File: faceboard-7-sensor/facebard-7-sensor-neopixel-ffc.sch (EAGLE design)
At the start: 42 parts, among them J1 1-1734592-4, J3 1-1734592-4, Q1 QRE1113, Q2 QRE1113, Q3 QRE1113, Q4 QRE1113, Q5 QRE1113, Q6 QRE1113, Q7 QRE1113, U1 CD4051BE

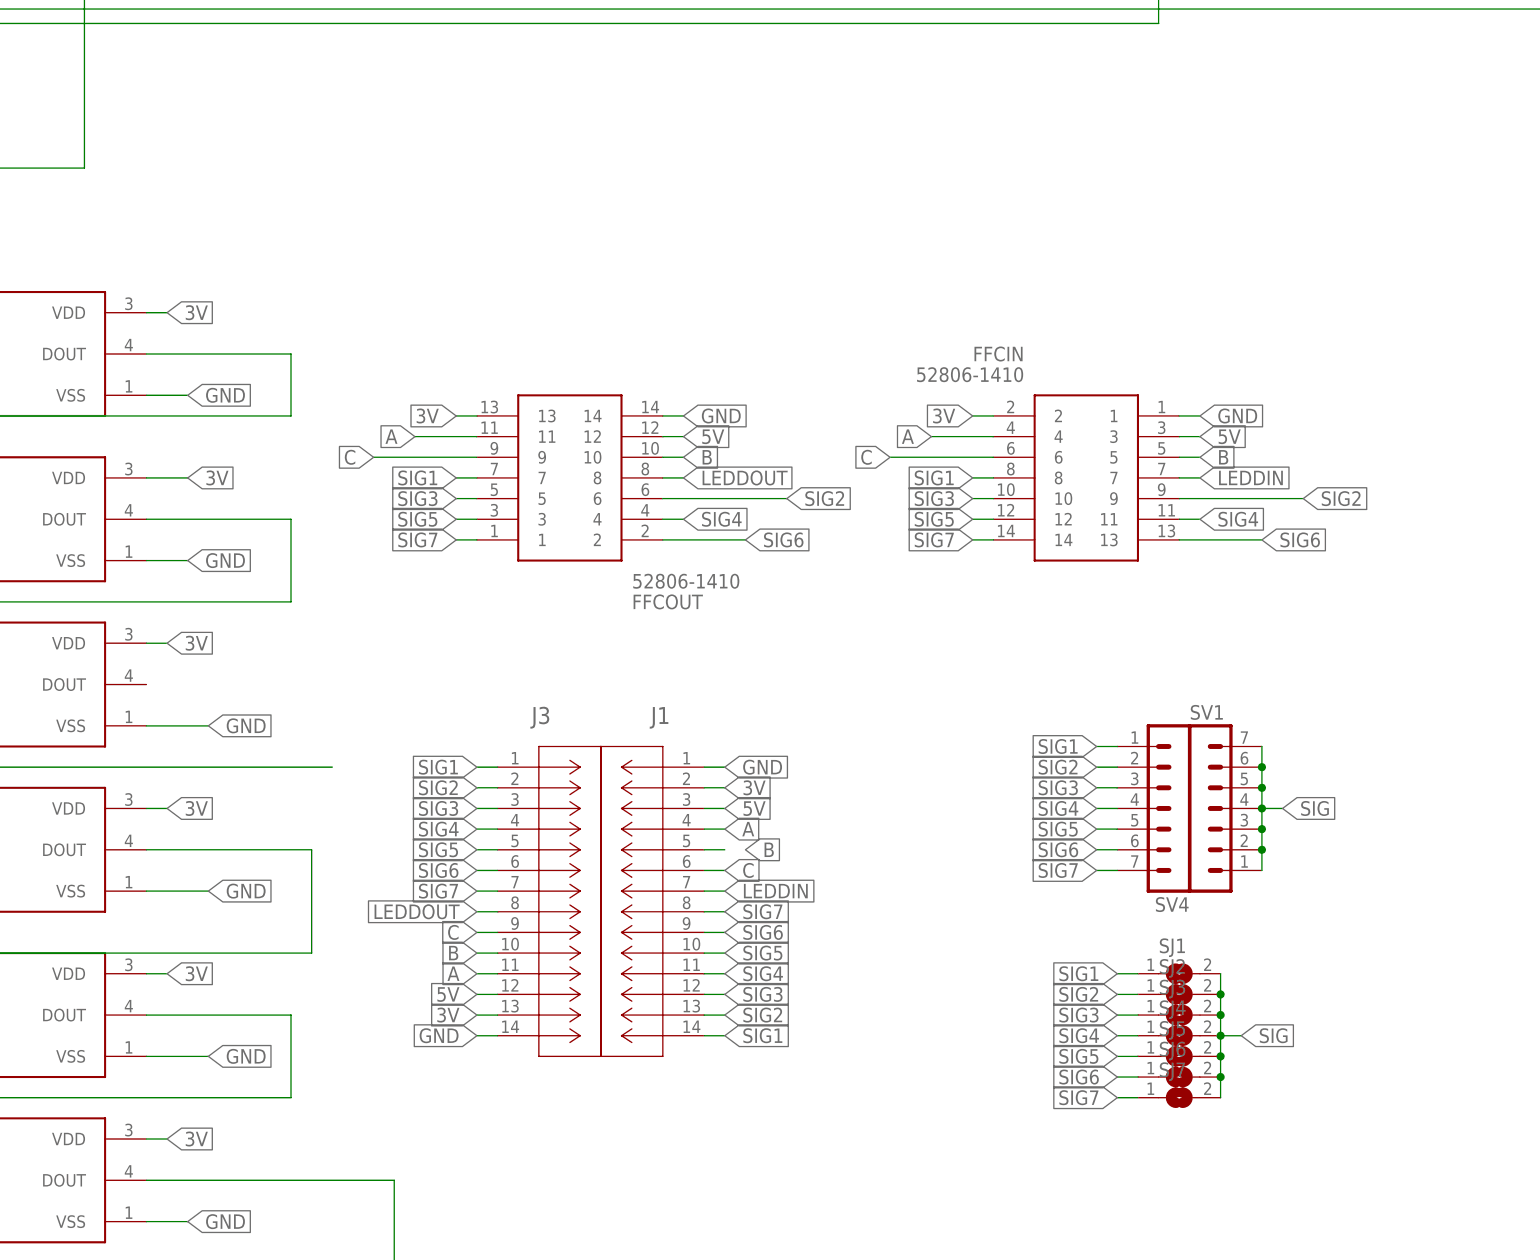
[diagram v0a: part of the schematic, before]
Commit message: remove 0.5mm ffc
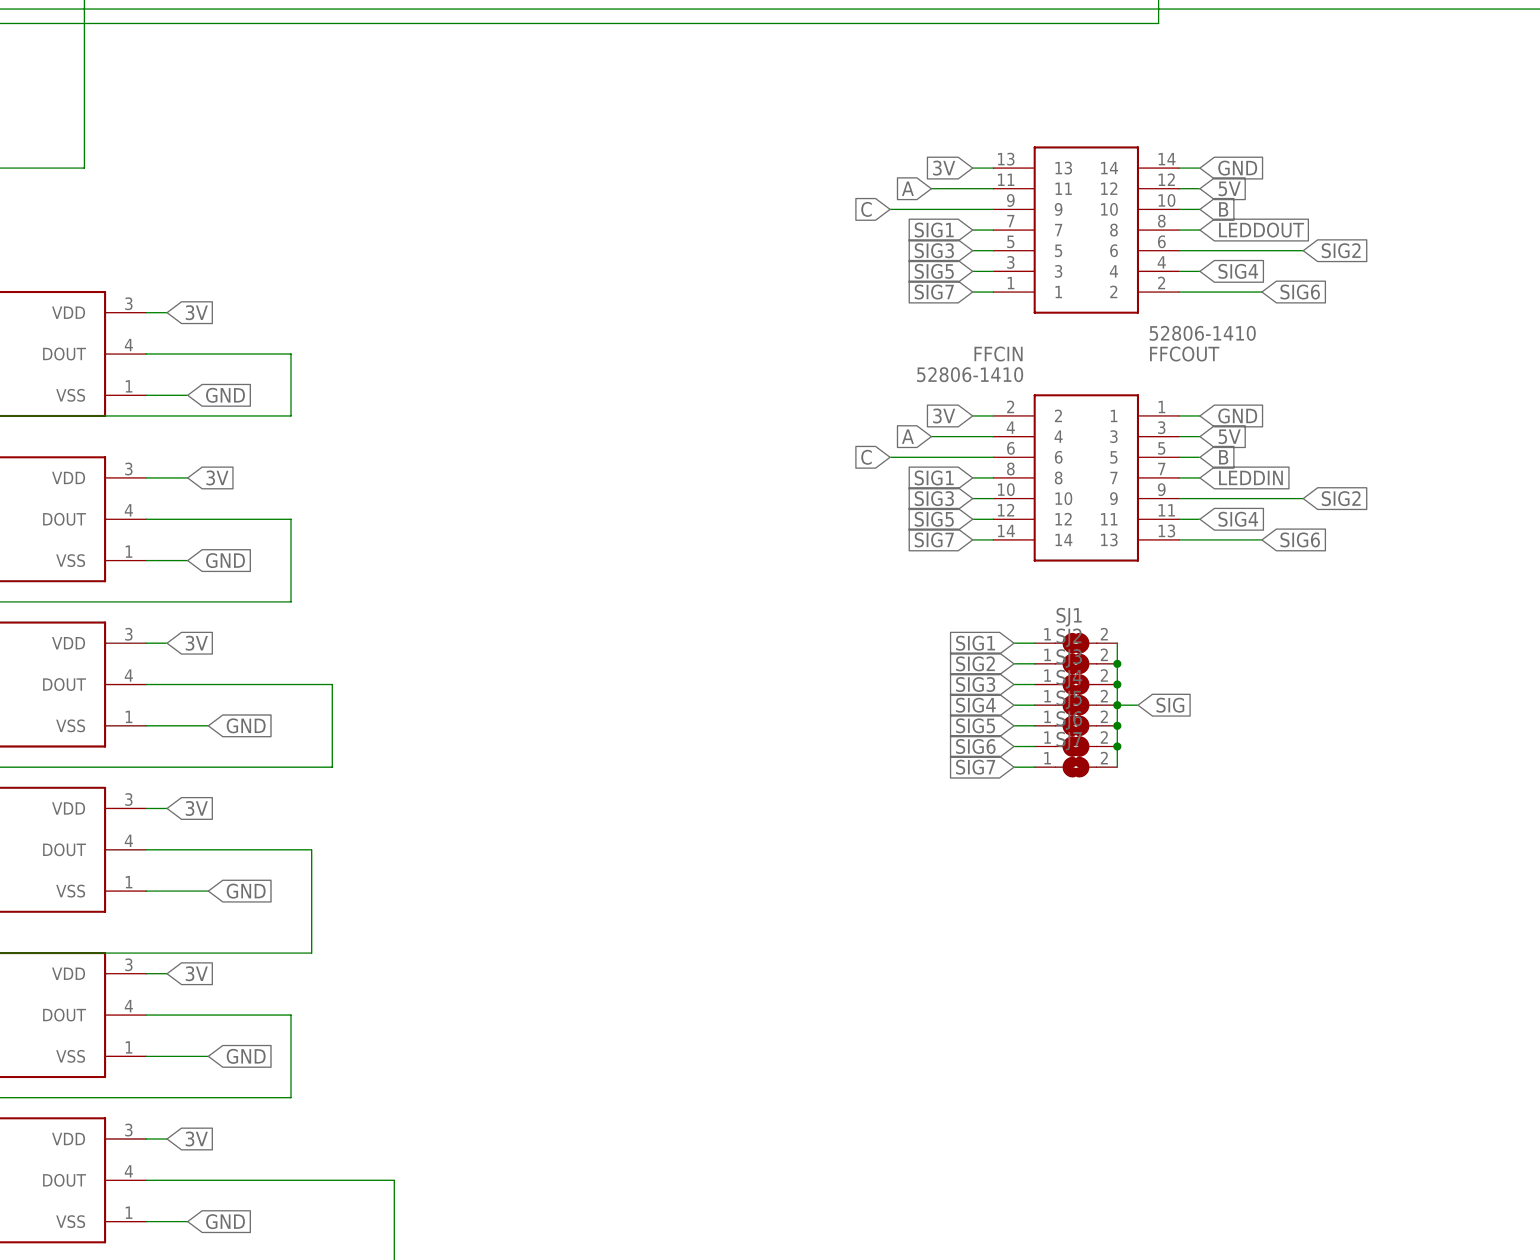
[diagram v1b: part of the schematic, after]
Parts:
- removed J1, J3: 1-1734592-4, 1-1734592-4:1-1734592-4
- removed SV1, SV4: (no value), con-lstb:MA07-1
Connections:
- net 3V: no longer J1.2, J3.13
- net 5V: no longer J1.3, J3.12
- net A: no longer J1.4, J3.11
- net B: no longer J1.5, J3.10
- net C: no longer J1.6, J3.9
- net GND: no longer J1.1, J3.14
- net LEDDIN: no longer J1.7
- net LEDDOUT: no longer J3.8
- net N$18: now also D3.DOUT
- net SIG: no longer SV1.1, SV1.2, SV1.3, SV1.4, SV1.5, SV1.6, SV1.7
- net SIG1: no longer J1.14, J3.1, SV4.1
- net SIG2: no longer J1.13, J3.2, SV4.2
- net SIG3: no longer J1.12, J3.3, SV4.3
- net SIG4: no longer J1.11, J3.4, SV4.4
- net SIG5: no longer J1.10, J3.5, SV4.5
- net SIG6: no longer J1.9, J3.6, SV4.6
- net SIG7: no longer J1.8, J3.7, SV4.7
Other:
- moved on the sheet: FFCOUT, SJ1, SJ2, SJ3, SJ4, SJ5, SJ6, SJ7

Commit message: add ffc boards
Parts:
- removed R10, R12, R14, R2, R4, R6, R8: 100k, rcl:R-EU_0207/10
- added RDV: 1M, rcl:R-EU_0207/10
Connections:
- net 3V: now also FFCIN.13, FFCOUT.2; no longer FFCIN.2, FFCOUT.13
- net 5V: now also FFCIN.12, FFCOUT.3, RDV.2; no longer FFCIN.3, FFCOUT.12, R10.2, R12.2, R14.2, R2.2, R4.2, R6.2, R8.2
- net A: now also FFCIN.11, FFCOUT.4; no longer FFCIN.4, FFCOUT.11
- net B: now also FFCIN.10, FFCOUT.5; no longer FFCIN.5, FFCOUT.10
- net C: now also FFCIN.9, FFCOUT.6; no longer FFCIN.6, FFCOUT.9
- net GND: now also FFCIN.14, FFCOUT.1; no longer FFCIN.1, FFCOUT.14
- net LEDDIN: now also FFCIN.8; no longer FFCIN.7
- net LEDDOUT: now also FFCOUT.7; no longer FFCOUT.8
- net Q1SIG: no longer R2.1
- net Q2SIG: no longer R4.1
- net Q3SIG: no longer R6.1
- net Q4SIG: no longer R8.1
- net Q5SIG: no longer R10.1
- net Q6SIG: no longer R12.1
- net Q7SIG: no longer R14.1
- net SIG: now also RDV.1
- net SIG1: now also FFCIN.7, FFCOUT.8; no longer FFCIN.8, FFCOUT.7
- net SIG2: now also FFCIN.6, FFCOUT.9; no longer FFCIN.9, FFCOUT.6
- net SIG3: now also FFCIN.5, FFCOUT.10; no longer FFCIN.10, FFCOUT.5
- net SIG4: now also FFCIN.4, FFCOUT.11; no longer FFCIN.11, FFCOUT.4
- net SIG5: now also FFCIN.3, FFCOUT.12; no longer FFCIN.12, FFCOUT.3
- net SIG6: now also FFCIN.2, FFCOUT.13; no longer FFCIN.13, FFCOUT.2
- net SIG7: now also FFCIN.1, FFCOUT.14; no longer FFCIN.14, FFCOUT.1
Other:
- moved on the sheet: FFCIN, FFCOUT

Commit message: tidy routing
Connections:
- net Q1SIG renamed C0
- net Q2SIG renamed C1
- net Q3SIG renamed C2
- net Q4SIG renamed C3
- net Q5SIG renamed C4
- net Q6SIG renamed C5
- net Q7SIG renamed C6

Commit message: change divide resistor value
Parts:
- RDV: value 1M -> 100k
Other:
- moved on the sheet: D1, D2, D3, D4, D5, D6, D7, FFCIN, FFCOUT, SJ1, SJ2, SJ3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

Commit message: re-draw schematics
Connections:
- net LEDDIN renamed DIN
- net LEDDOUT renamed DOUT
- net SIG1 renamed S1
- net SIG2 renamed S2
- net SIG3 renamed S3
- net SIG4 renamed S4
- net SIG5 renamed S5
- net SIG6 renamed S6
- net SIG7 renamed S7
- removed net 5V: FFCIN.12, FFCOUT.3, R1.1, R11.1, R13.1, R3.1, R5.1, R7.1, R9.1, RDV.2, U1.VDD
- removed net N$9: Q5.1, R9.2
- new net N$2: FFCOUT.3, R1.1, R11.1, R13.1, R3.1, R5.1, R7.1, R9.1
- new net VCC: FFCIN.12, RDV.2, U1.VDD
- net C0: now also U1.CH0; no longer U1.CHANNELSIN/OUT0
- net C1: now also U1.CH1; no longer U1.CHANNELSIN/OUT1
- net C2: now also U1.CH2; no longer U1.CHANNELSIN/OUT2
- net C3: now also U1.CH3; no longer U1.CHANNELSIN/OUT3
- net C4: now also U1.CH4; no longer U1.CHANNELSIN/OUT4
- net C5: now also U1.CH5; no longer U1.CHANNELSIN/OUT5
- net C6: now also U1.CH6; no longer U1.CHANNELSIN/OUT6
- net GND: now also U1.GND; no longer FFCIN.14, U1.VSS
- net SIG: now also U1.COM; no longer U1.COMOUT/IN
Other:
- note added: "Soulder Junction"
- moved on the sheet: D1, D2, D3, D4, D5, D6, D7, FFCIN, FFCOUT, R1, R11, R13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
